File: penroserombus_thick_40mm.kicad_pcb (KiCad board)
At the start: 2 copper layers, 52.4 x 38 mm, 21 parts, among them J1 Conn_01x03_Female, J2 Conn_01x03_Female, J3 Conn_01x03_Male, J4 Conn_01x03_Male, M3 MountingHole_3.2mm_M3_ISO7380, SW1 SW_DPDT_x2

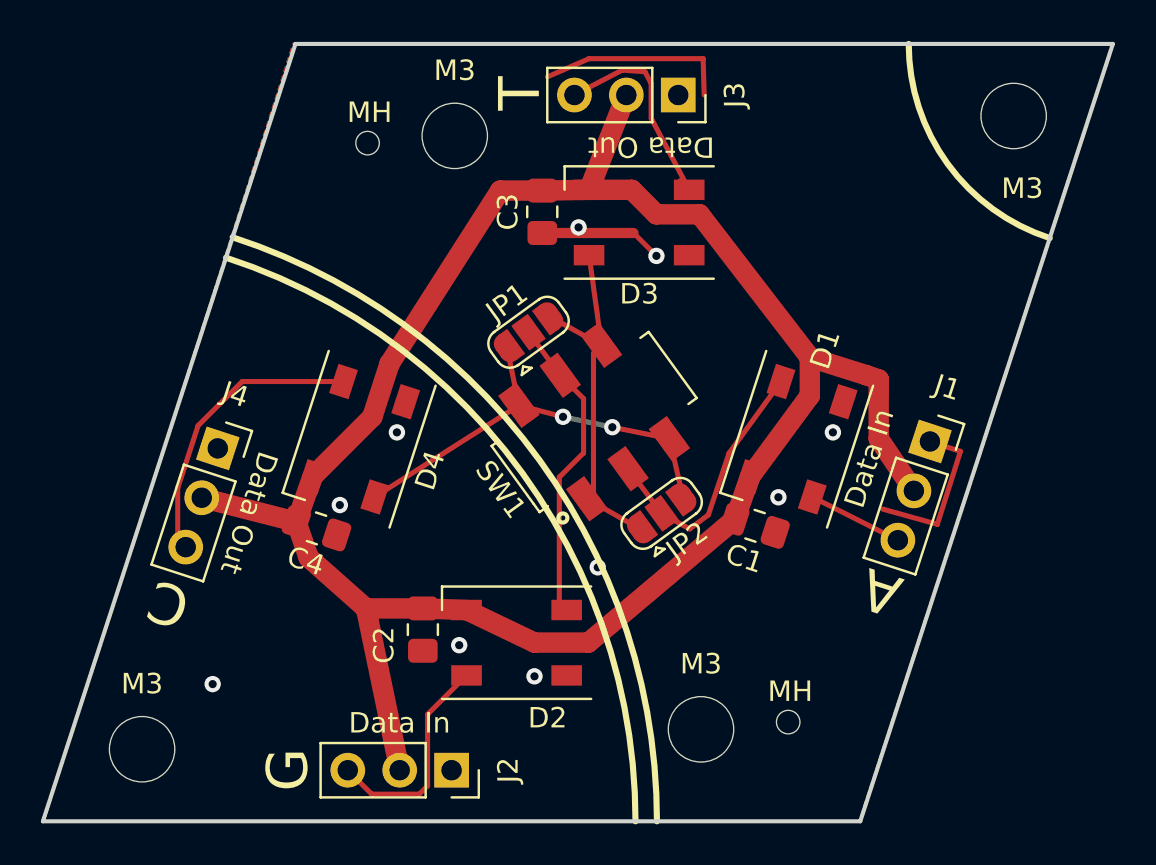
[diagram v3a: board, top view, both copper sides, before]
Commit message: board wiring changes and mounting hole additions for adhesive standoffs
changed top copper fill to VCC and added mounting holes with new footprint to check if the mounts collided.
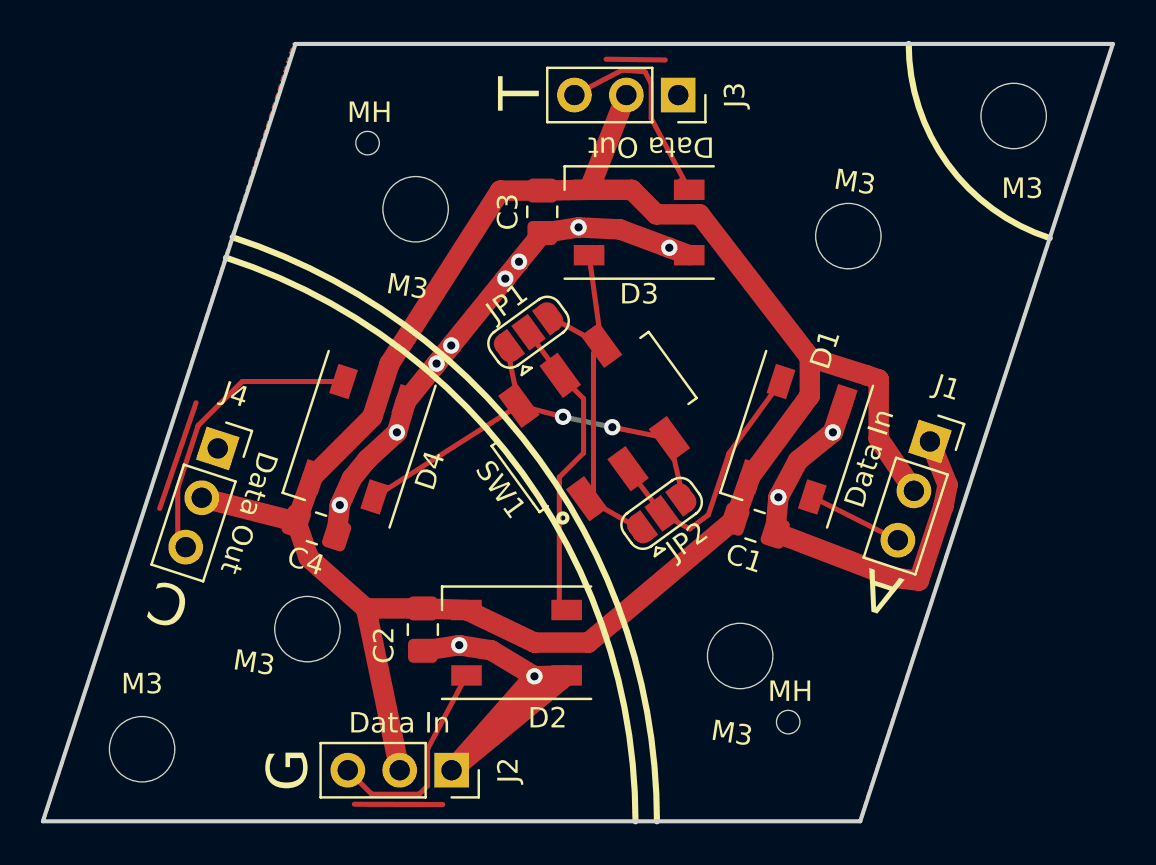
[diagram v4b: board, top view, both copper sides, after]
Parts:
- removed the M3 at (153.1, 109.5)
- removed the M3 at (141.0, 80.5)
- added M3: HC-5Nylonadhesiveclip, penroserombus:HC-5Nylonadhesiveclip, F.Cu at (155.0, 105.9)
- added M3: HC-5Nylonadhesiveclip, penroserombus:HC-5Nylonadhesiveclip, F.Cu at (139.1, 84.1)
- added M3: HC-5Nylonadhesiveclip, penroserombus:HC-5Nylonadhesiveclip, F.Cu at (133.8, 104.6)
- added M3: HC-5Nylonadhesiveclip, penroserombus:HC-5Nylonadhesiveclip, F.Cu at (160.3, 85.4)
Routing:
- net GND: track 23.7 -> 68.7 mm, vias 10 -> 12
- net VCC: track 101.4 -> 114.1 mm
- added copper zone on F.Cu, net VCC
- removed copper zone on F.Cu, net GND

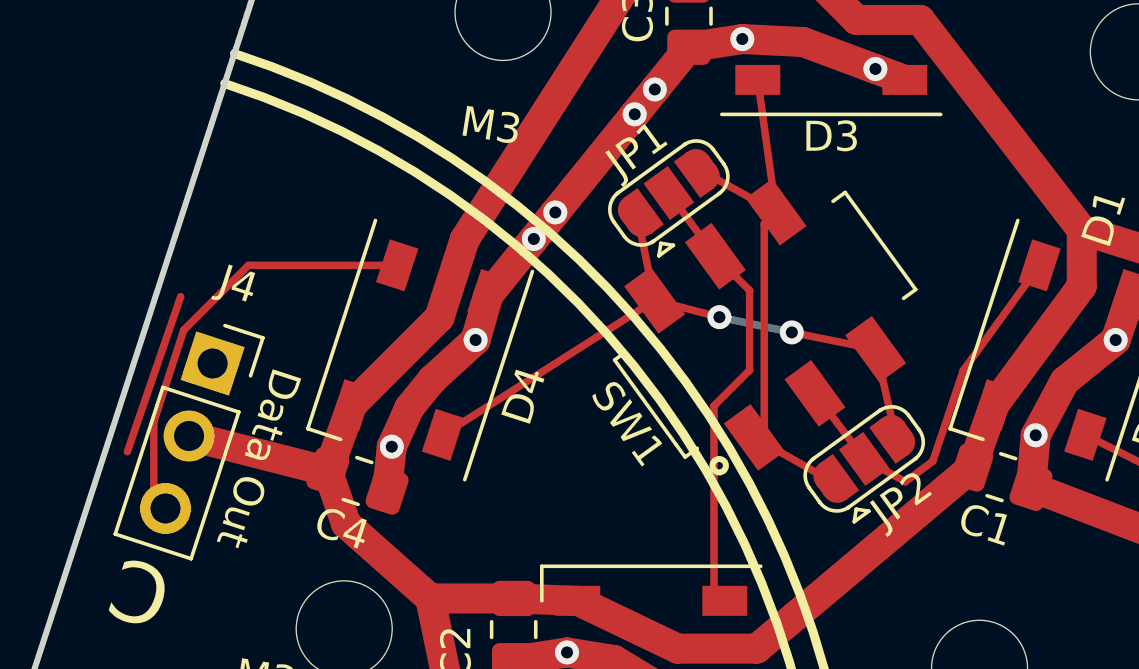
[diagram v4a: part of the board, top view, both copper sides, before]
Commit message: minor tweaks and diagrams
Tweaks to silkscreen and stuff also added a diagram to explain switch on board. Also made top layer VCC on penrose kite.
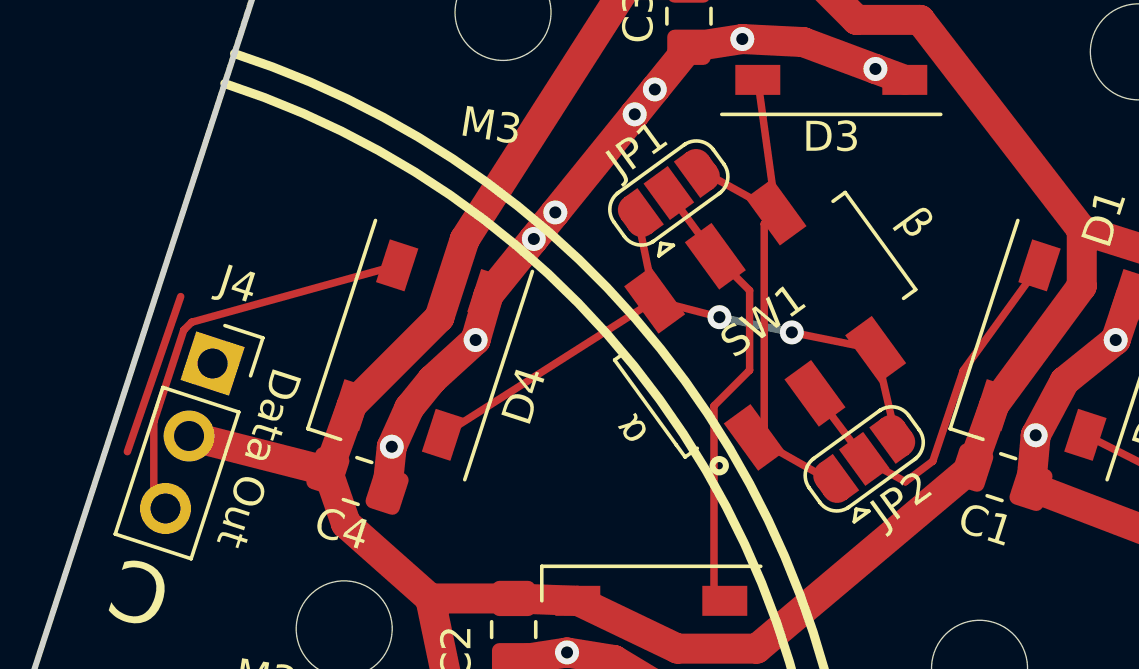
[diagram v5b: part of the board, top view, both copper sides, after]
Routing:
- net Net-(D4-Pad4): track 14.3 -> 13.7 mm
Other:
- board text added: "α"
- board text added: "β"
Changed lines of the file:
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@@
   (general
     (thickness 1.6)
-    (drawings 32)
+    (drawings 34)
     (tracks 114)
     (zones 0)
@@
   (module penroserombus:Aliexpress_slideswitch_2P2T (layer F.Cu)
     (at 147.828 94.488 126)
-    (fp_text reference SW1 (at 0.01598 -5.639693 126) (layer F.SilkS)
+    (fp_text reference SW1 (at 0.153892 0.030179 216) (layer F.SilkS)
       (effects (font (size 1 1) (thickness 0.15)))
     )
@@
       (rotate (xyz 0 0 0))
     )
+  )
+  (gr_text α (at 143.3576 98.00336 126) (layer F.SilkS)
+    (effects (font (size 1 1) (thickness 0.15)))
+  )
+  (gr_text β (at 152.86228 91.07932 306) (layer F.SilkS)
+    (effects (font (size 1 1) (thickness 0.15)))
   )
   (gr_text "Gnd\nVcc\nData" (at 129.5908 98.679 342) (layer B.SilkS)
@@
   (segment (start 150.622 79.629) (end 150.622 77.9272) (width 0.25) (layer F.Cu) (net 8))
   (segment (start 150.313814 77.346386) (end 149.1996 77.2668) (width 0.25) (layer F.Cu) (net 8))
-  (segment (start 130.605662 92.507179) (end 135.561695 92.507179) (width 0.25) (layer F.Cu) (net 9))
   (segment (start 127.839795 100.611039) (end 127.449697 100.220941) (width 0.25) (layer F.Cu) (net 9))
   (segment (start 127.449697 100.220941) (end 127.449697 97.721303) (width 0.25) (layer F.Cu) (net 9))
   (segment (start 127.449697 97.721303) (end 128.447421 94.665421) (width 0.25) (layer F.Cu) (net 9))
-  (segment (start 128.447421 94.665421) (end 130.605662 92.507179) (width 0.25) (layer F.Cu) (net 9))
+  (segment (start 135.561695 92.507179) (end 128.709041 94.403801) (width 0.25) (layer F.Cu) (net 9))
+  (segment (start 128.447421 94.665421) (end 128.709041 94.403801) (width 0.25) (layer F.Cu) (net 9))
   (via (at 148.717 94.742) (size 0.8) (drill 0.4) (layers F.Cu B.Cu) (net 10))
   (segment (start 148.717 94.742) (end 151.511036 95.30401) (width 0.25) (layer F.Cu) (net 10) (status 20))

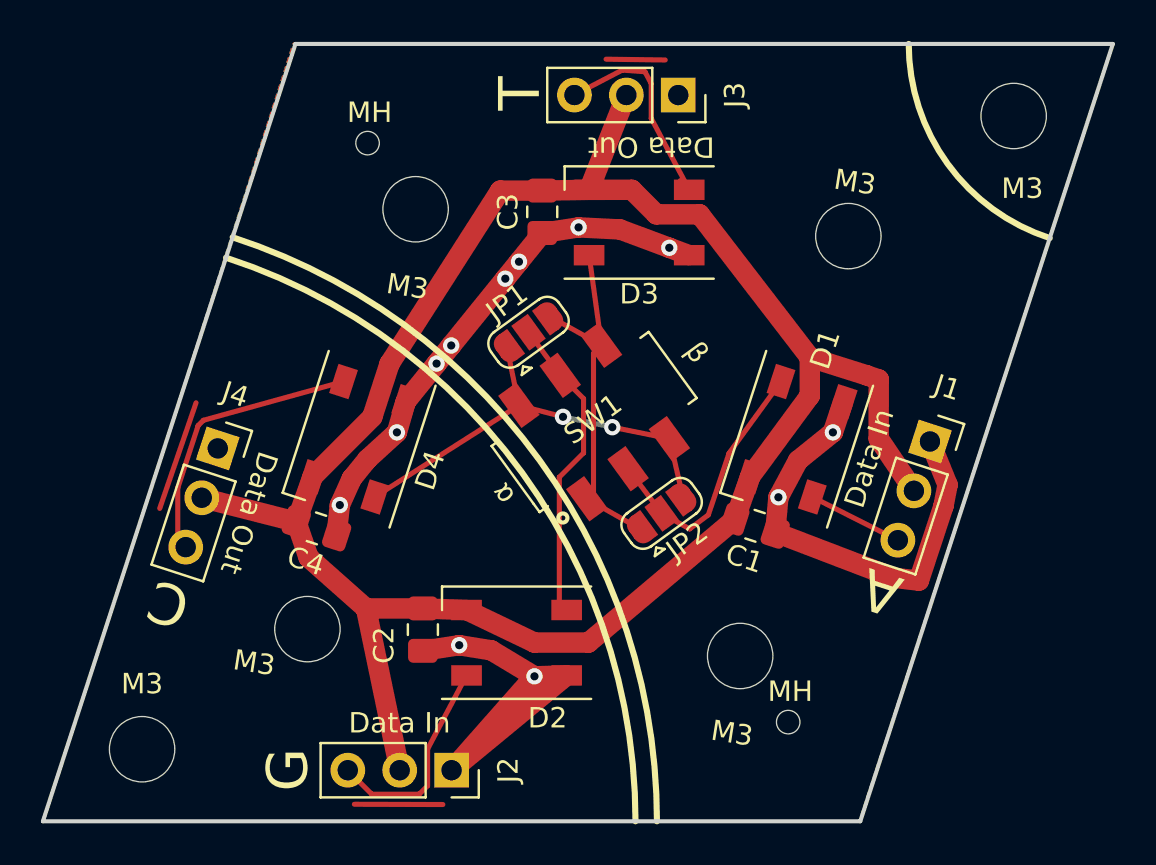
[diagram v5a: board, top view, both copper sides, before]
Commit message: added even more mounting holes
honestly these boards are starting to look like swiss cheese but seeing how prototyping is expensive, I want to have my bases covered.
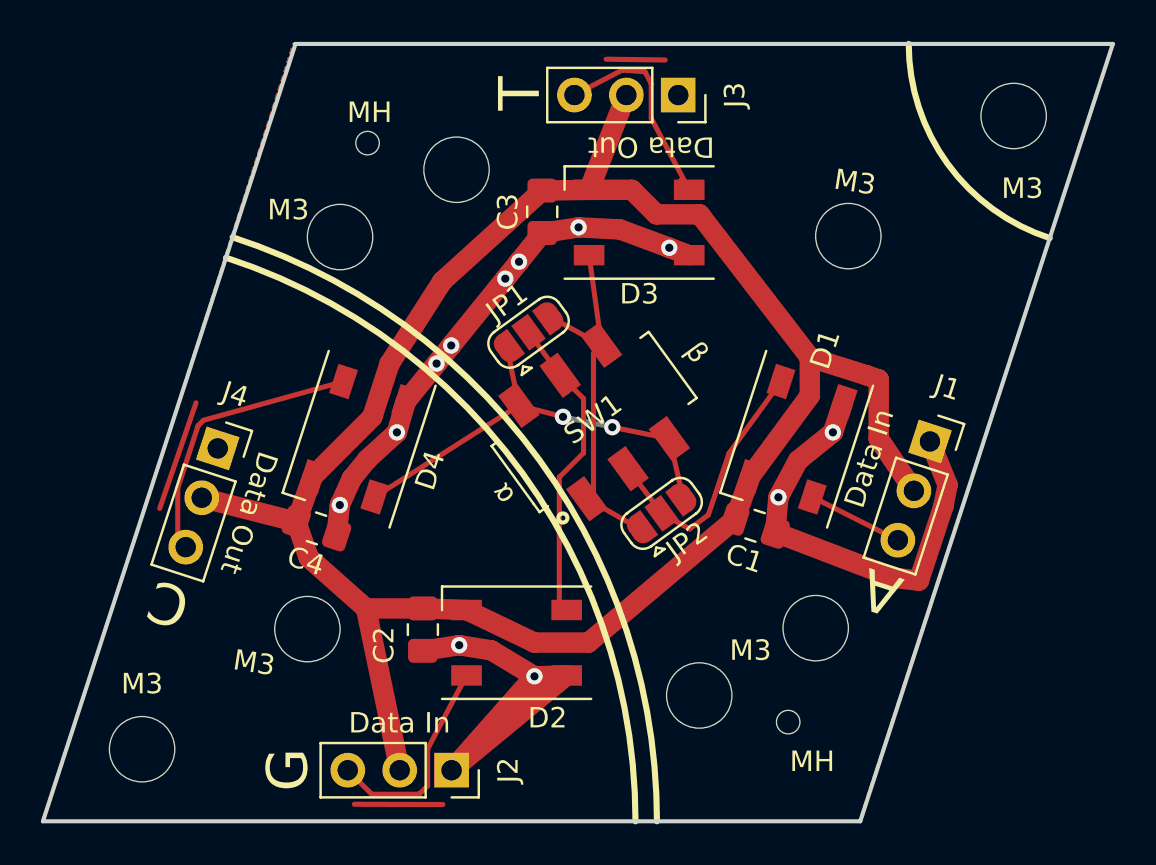
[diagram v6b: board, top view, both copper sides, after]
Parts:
- removed the M3 at (155.0, 105.9)
- removed the M3 at (139.1, 84.1)
- added M3: MountingHole_3.2mm_M3_ISO7380, MountingHole:MountingHole_3.2mm_M3_ISO7380, F.Cu at (158.7, 104.6)
- added M3: MountingHole_3.2mm_M3_ISO7380, MountingHole:MountingHole_3.2mm_M3_ISO7380, F.Cu at (135.4, 85.4)
- added M3: HC-5Nylonadhesiveclip, penroserombus:HC-5Nylonadhesiveclip, F.Cu at (153.0, 107.9)
- added M3: HC-5Nylonadhesiveclip, penroserombus:HC-5Nylonadhesiveclip, F.Cu at (141.1, 82.1)
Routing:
- net VCC: track 114.1 -> 113.4 mm
